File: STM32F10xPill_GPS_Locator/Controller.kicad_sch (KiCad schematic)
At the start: 27 parts, among them J2 Conn_01x03, J3 Conn_01x05, SW1 SW_Push, U1 STM32F100C4Tx, Y1 16MHz, Y2 32.768kHz

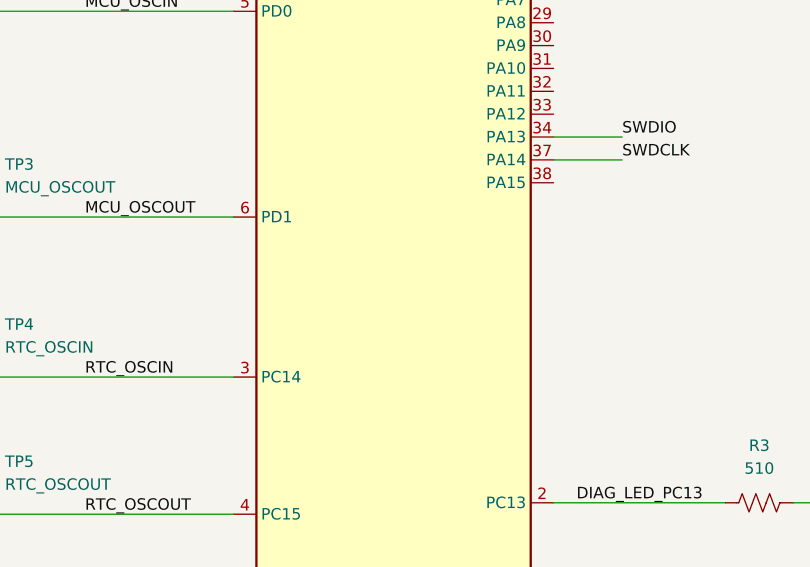
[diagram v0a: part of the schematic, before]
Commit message: Add library parts for peripherals
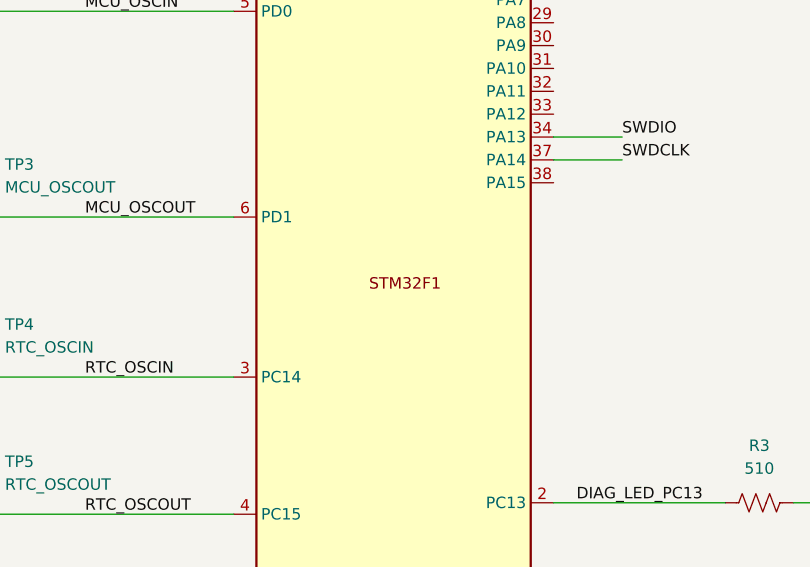
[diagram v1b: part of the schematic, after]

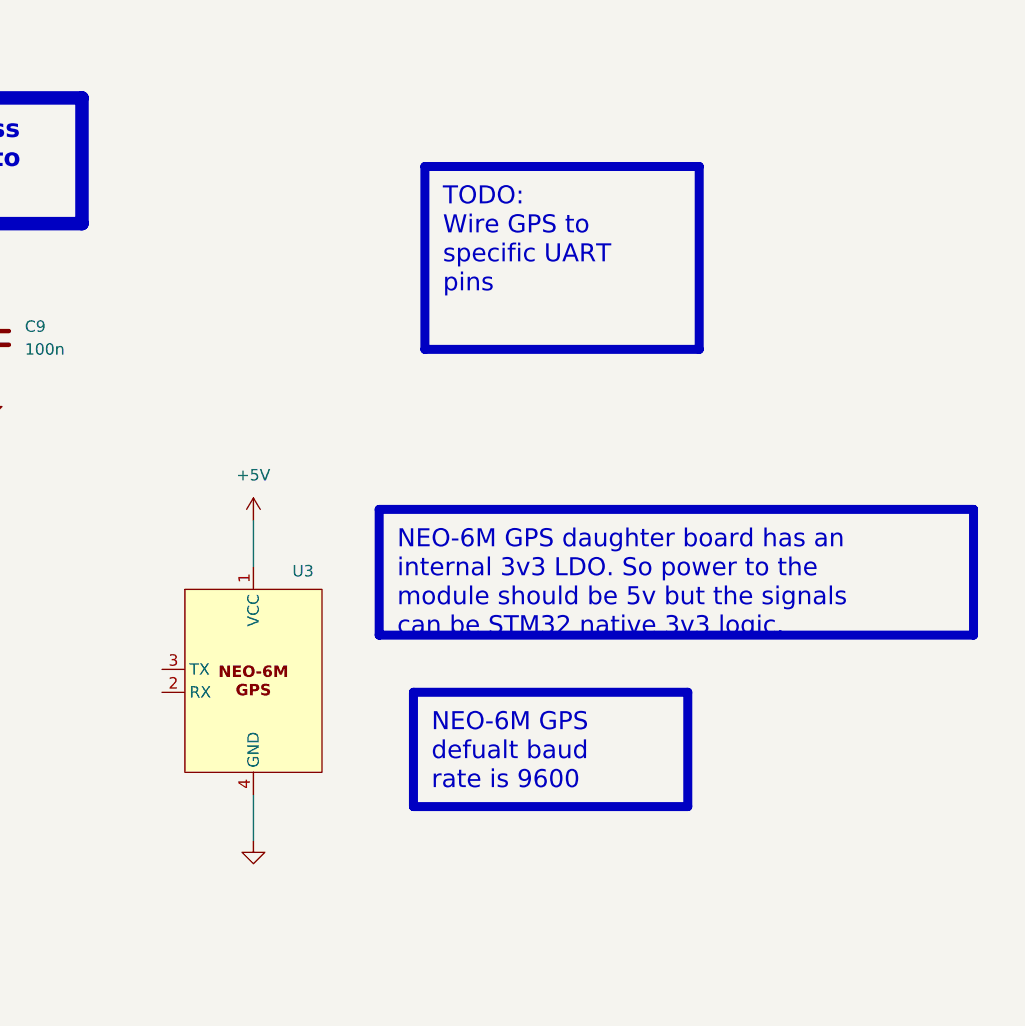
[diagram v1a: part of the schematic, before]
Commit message: Switch from NEO-6m GPS to ATGM336H-5N31
The neo-6m is EOL and not readily available as an IC module
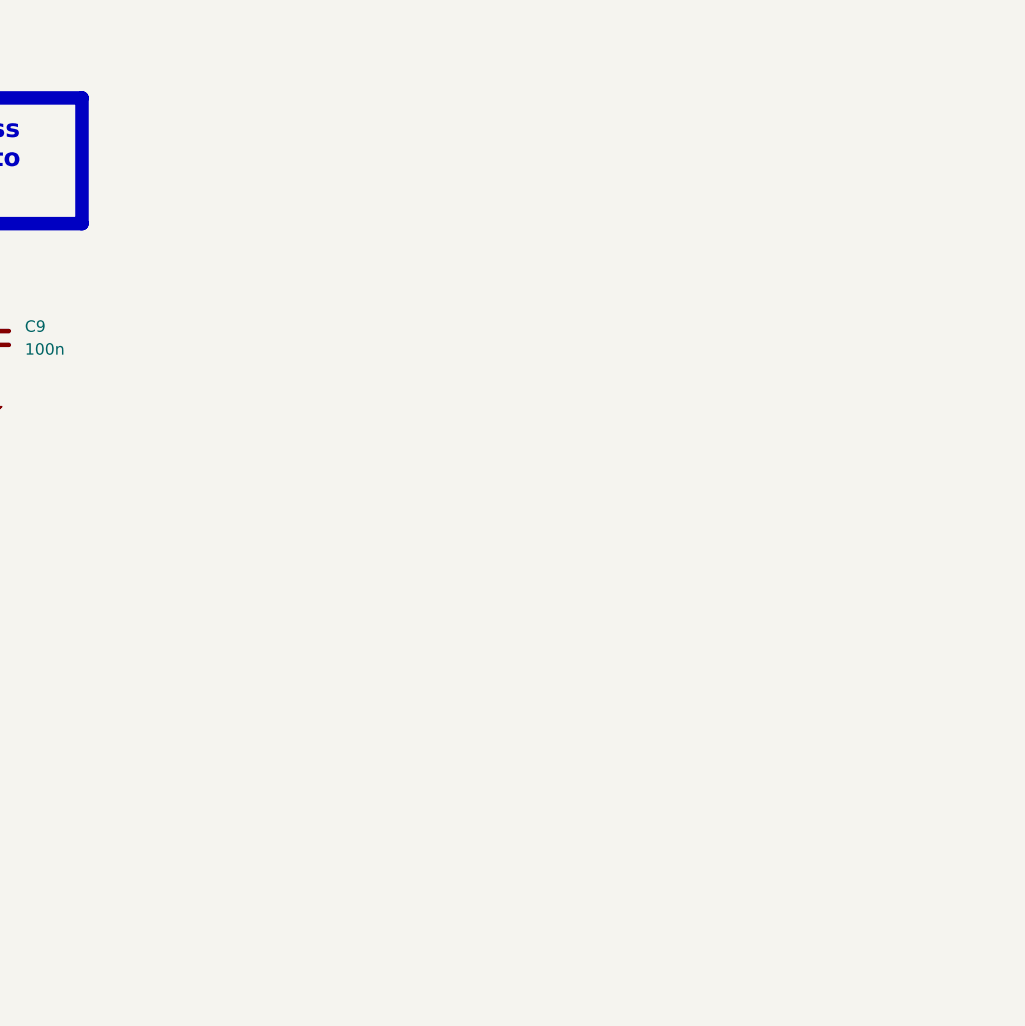
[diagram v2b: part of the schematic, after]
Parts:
- removed U3: ~, symbol Modules:NEO-6M_Daughter_Board

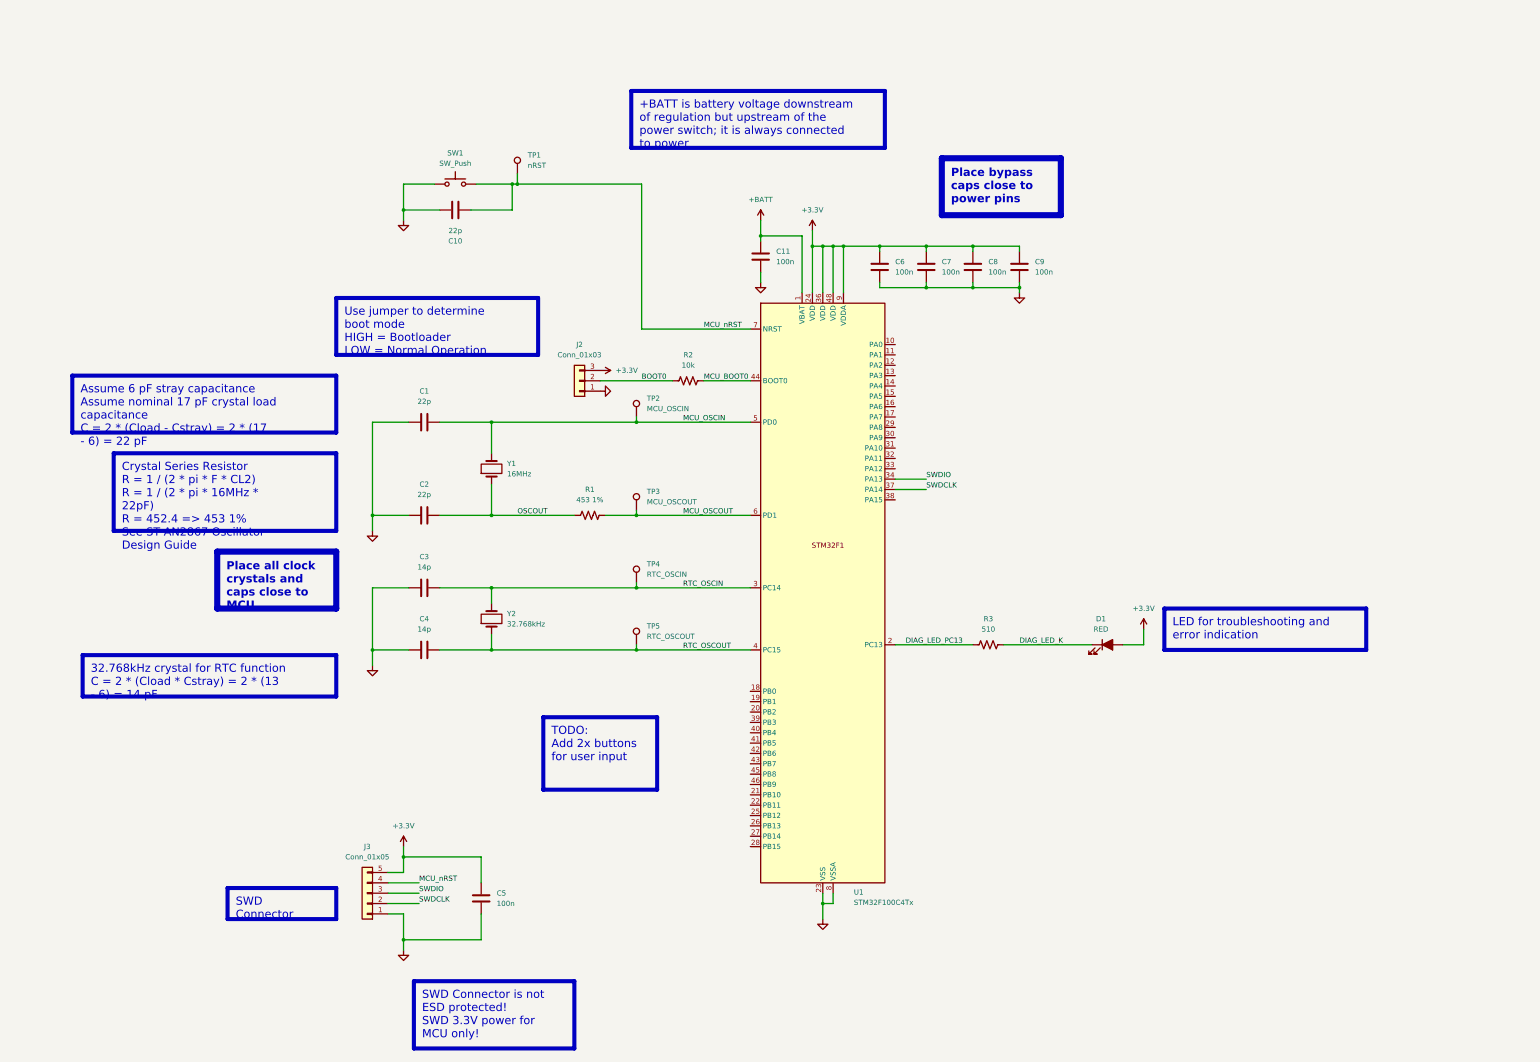
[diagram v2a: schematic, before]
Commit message: Work on adding GPS and Compass Peripherals
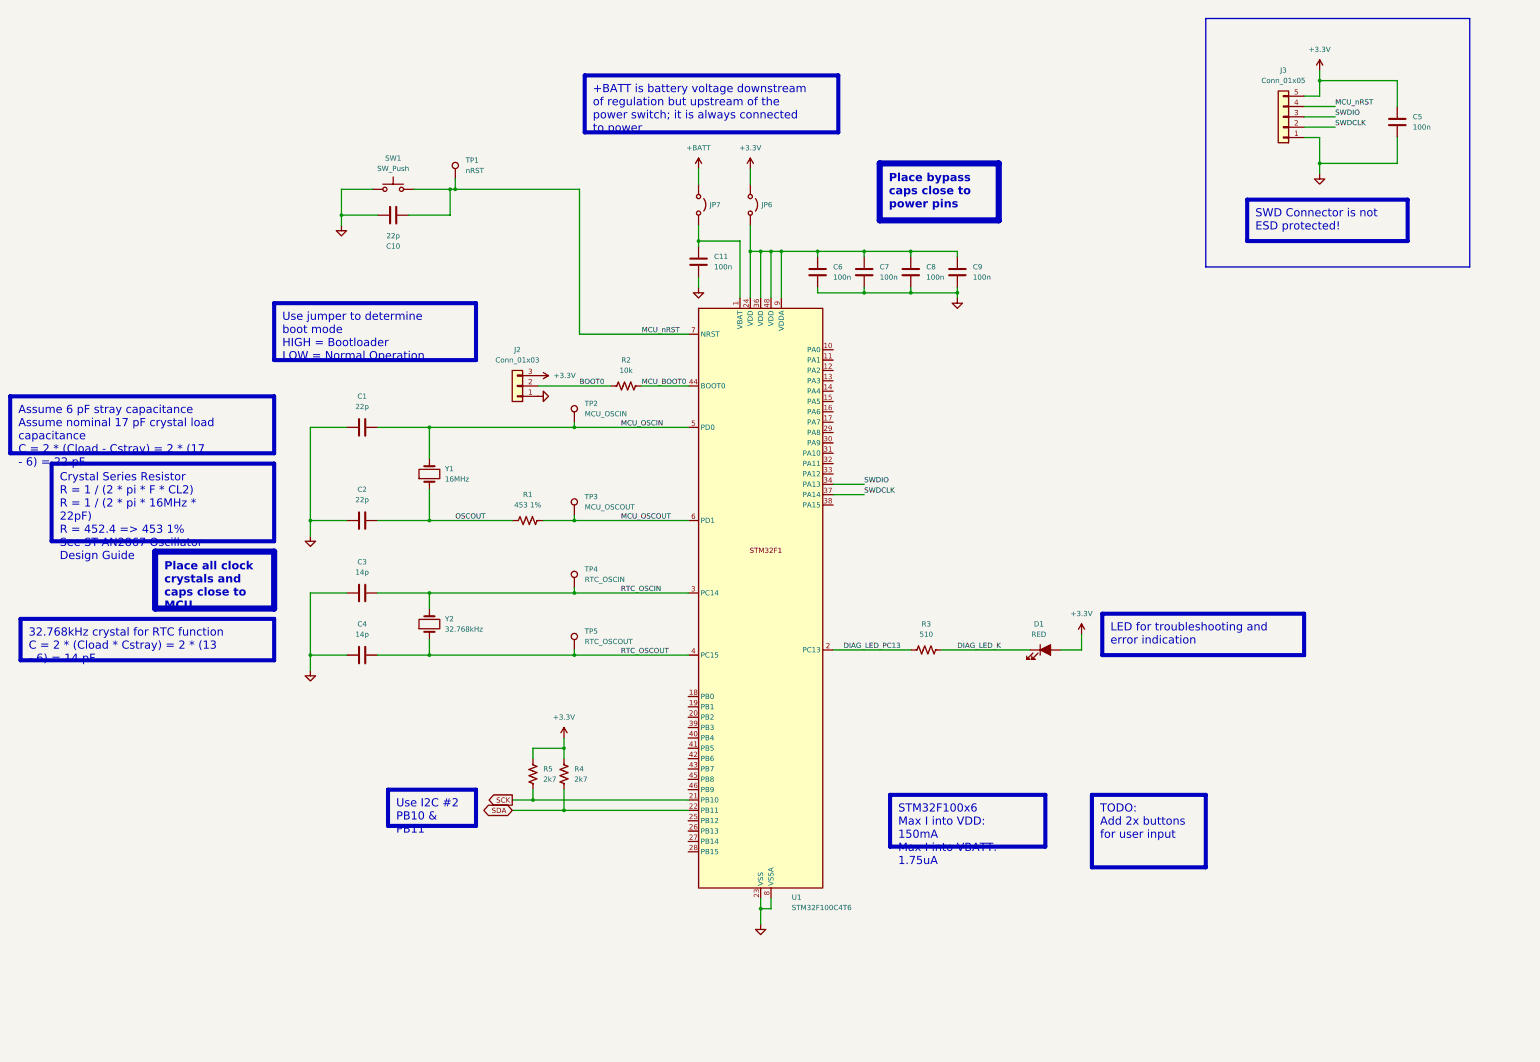
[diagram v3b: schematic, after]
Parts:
- added JP6, JP7: Jumper_2_Open, symbol Jumper:Jumper_2_Open
- added R4, R5: 2k7, symbol Device:R_US
- U1: value STM32F100C4Tx -> STM32F100C4T6
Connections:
- net +3.3V: now also JP6.1 (A), R4.2, R5.2; no longer C6.2, C7.2, C8.2, C9.2, U1.24 (VDD), U1.36 (VDD), U1.48 (VDD), U1.9 (VDDA)
- net +BATT: now also JP7.1 (A); no longer C11.2, U1.1 (VBAT)
- net SCK: now reaches U1.21 (PB10)
- net SCK: now also R5.1
- net SDA: now reaches U1.22 (PB11)
- net SDA: now also R4.1
- new net: C6.2, C7.2, C8.2, C9.2, JP6.2 (B), U1.24 (VDD), U1.36 (VDD), U1.48 (VDD), U1.9 (VDDA)
- new net: C11.2, JP7.2 (B), U1.1 (VBAT)
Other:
- moved on the sheet: C1, C10, C11, C2, C3, C4, C5, C6, C7, C8, C9, D1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

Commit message: Schematic is largely complete
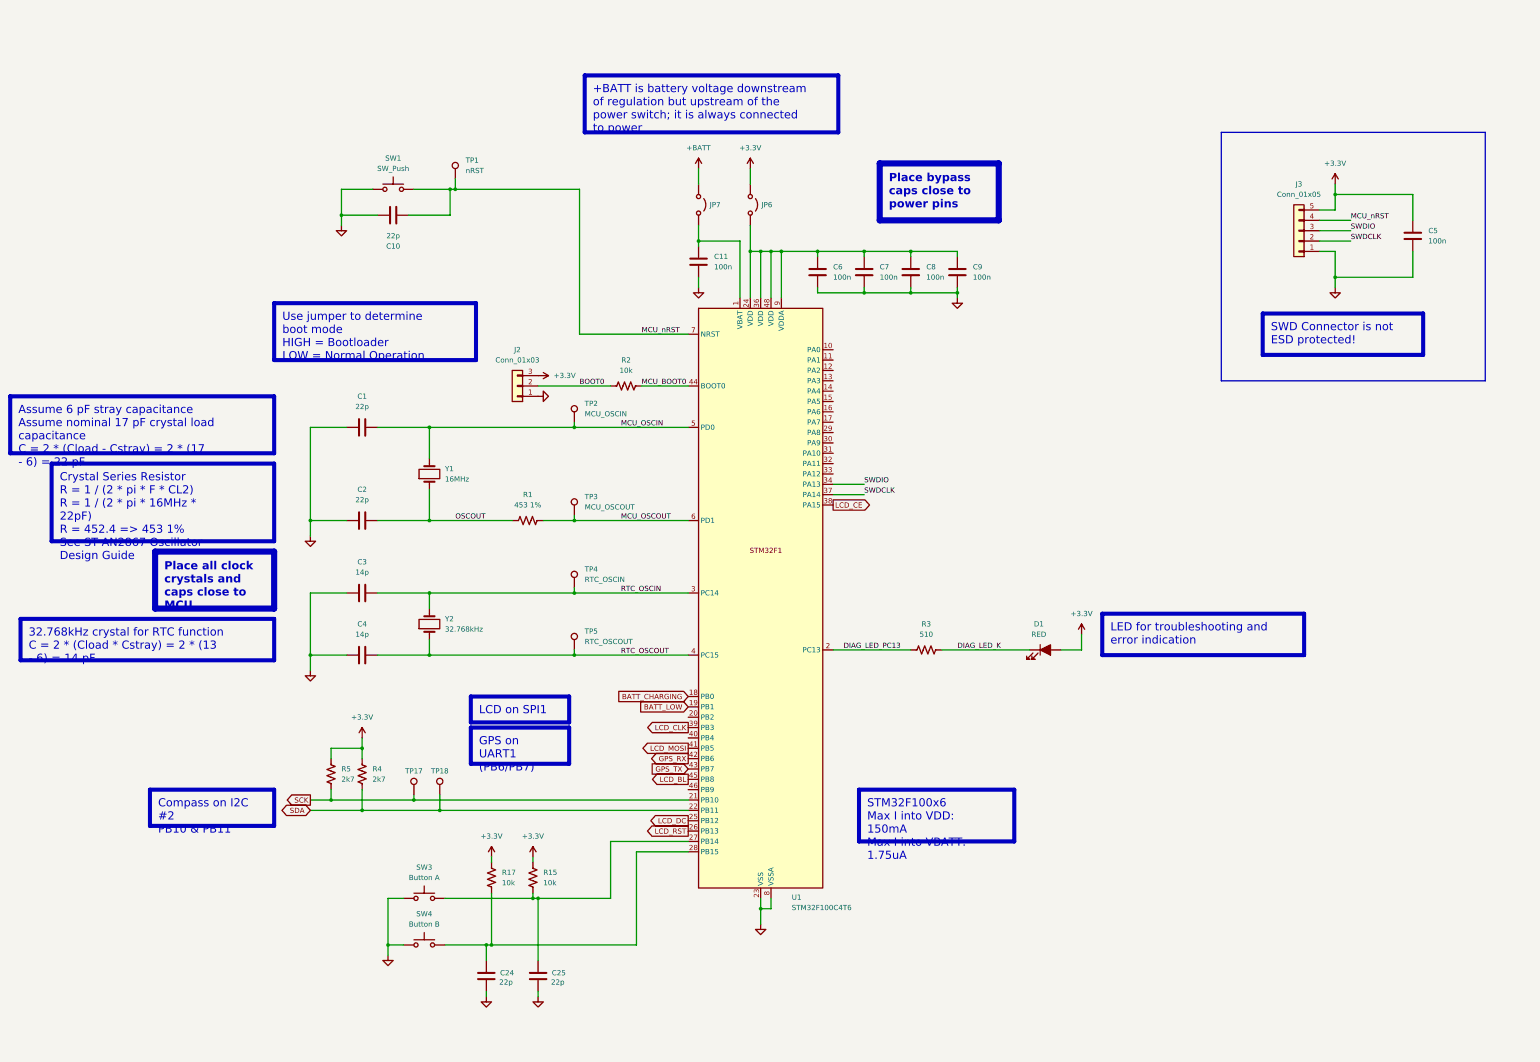
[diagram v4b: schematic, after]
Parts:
- added C24, C25: 22p, symbol Device:C
- added R15, R17: 10k, symbol Device:R_US
- added SW3: Button A, symbol Switch:SW_Push
- added SW4: Button B, symbol Switch:SW_Push
- added TP17, TP18: GPS_1PPS, symbol Connector:TestPoint
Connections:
- net +3.3V: now also R15.2, R17.2
- net GND: now also C24.1, C25.1, SW3.1, SW4.1
- net SCK: now also TP17.1
- net SDA: now also TP18.1
- net BATT_CHARGING: now reaches U1.18 (PB0)
- net BATT_LOW: now reaches U1.19 (PB1)
- net LCD_DC: now reaches U1.25 (PB12)
- net LCD_RST: now reaches U1.26 (PB13)
- net at U1.27 (PB14): now also C25.2, R15.1, SW3.2
- net at U1.28 (PB15): now also C24.2, R17.1, SW4.2
- net LCD_CE: now reaches U1.38 (PA15)
- net LCD_CLK: now reaches U1.39 (PB3)
- net LCD_MOSI: now reaches U1.41 (PB5)
- net GPS_RX: now reaches U1.42 (PB6)
- net GPS_TX: now reaches U1.43 (PB7)
- net LCD_BL: now reaches U1.45 (PB8)
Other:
- moved on the sheet: C5, J3, R4, R5
